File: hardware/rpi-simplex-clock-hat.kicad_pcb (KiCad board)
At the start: 2 copper layers, 65 x 56 mm, 23 parts, among them J1 TBP01R1-508-04BE, J2 Barrel_Jack_Switch, J3 GPIO, U1 LAA120, U2 CAT24C256

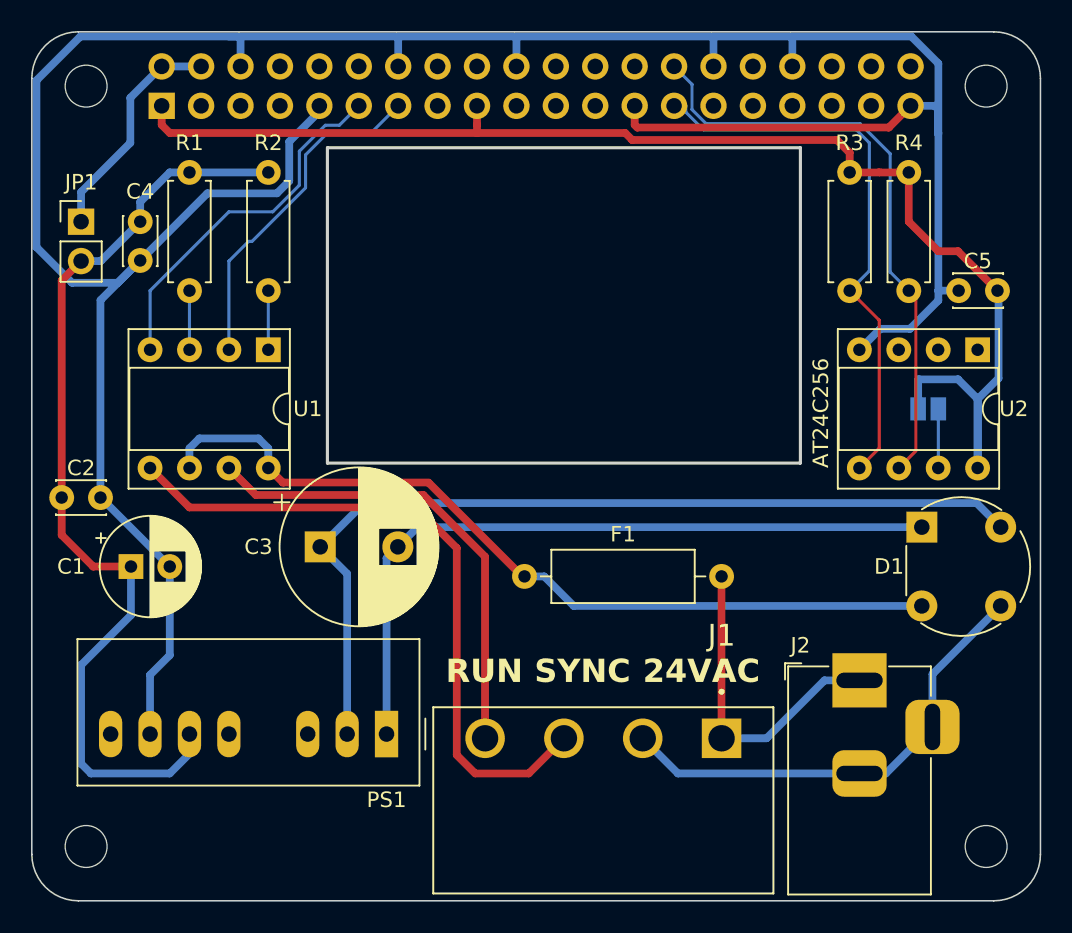
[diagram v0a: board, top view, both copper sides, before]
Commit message: Rev 1: Fix minor issues in Rev 0.
1. Turn SSRs on with logic 1 to GPIO outputs.  This is needed so that
   the SSRs don't become enabled when the GPIO17 and GPIO27 are set to
   outputs.  These GPIOs are pulled low.

2. Add alternate footprint location (J4) for AC input barrel jack.

3. Add additional mounting holes for Raspberry Pi Zero / Zero 2 W.

4. Correct pinout for the bridge rectifier D1.
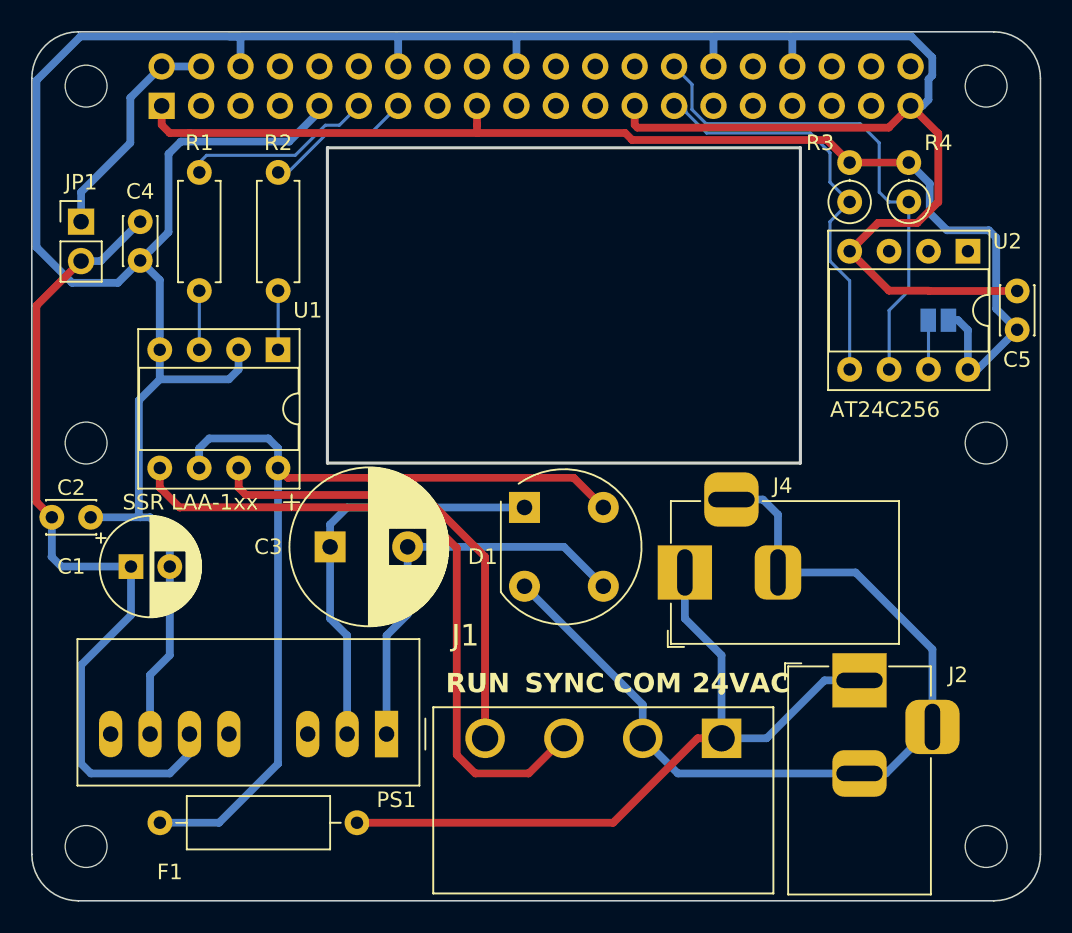
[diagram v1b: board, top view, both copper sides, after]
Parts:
- added J4: Barrel_Jack_Switch, Connector_BarrelJack:BarrelJack_Horizontal, F.Cu at (142.1, 78.8)
- added MH5: MountingHole_2.7mm_M2.5, MountingHole:MountingHole_2.7mm_M2.5, F.Cu at (103.5, 70.5)
- added MH6: MountingHole_2.7mm_M2.5, MountingHole:MountingHole_2.7mm_M2.5, F.Cu at (161.5, 70.5)
- D1: value D_Bridge_-AA+ -> B250C1000G-E4/51; footprint Diode_THT:Diode_Bridge_Round_D8.9mm -> Diode_THT:Diode_Bridge_Round_D9.8mm
- R1, R2: value 330 -> 220
- R3, R4: footprint Resistor_THT:R_Axial_DIN0207_L6.3mm_D2.5mm_P7.62mm_Horizontal -> Resistor_THT:R_Axial_DIN0207_L6.3mm_D2.5mm_P2.54mm_Vertical
- moved F1 28.4 mm to (108.3, 94.9)
- moved D1 25.6 mm to (131.8, 74.6)
- moved U2 6.38 mm to (160.3, 58.1)
- moved JP2 5.75 mm to (158.4, 62.5), turned to 0 degrees
- moved R3 5.72 mm to (152.7, 54.9)
- moved R4 5.72 mm to (156.5, 54.9)
- moved C5 2.82 mm to (163.5, 63.1), turned to 90 degrees
- moved C2 1.42 mm to (101.3, 75.2)
- moved C3 0.64 mm to (119.2, 77.1)
- moved R1 0.64 mm to (110.8, 60.6)
- moved R2 0.64 mm to (115.9, 60.6)
- moved U1 0.62 mm to (115.9, 64.4)
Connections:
- D1 pad 1: /COM -> +48V
- D1 pad 2: AC -> Net-(D1-Pad2)
- D1 pad 3: Net-(D1-Pad3) -> /COM
- D1 pad 4: +48V -> AC
- J1 pad 2: Net-(D1-Pad3) -> Net-(D1-Pad2)
- J2 pad 2: Net-(D1-Pad3) -> Net-(D1-Pad2)
- J2 pad 3: Net-(D1-Pad3) -> Net-(D1-Pad2)
- R1 pad 2: +5V -> /GPIO17
- R2 pad 2: +5V -> /GPIO27
- U1 pad 2: /GPIO27 -> GND
- U1 pad 4: /GPIO17 -> GND
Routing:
- net Net-(D1-Pad2): track 0.00 -> 57.9 mm
- net +48V: track 58.4 -> 26.9 mm
- net Net-(D1-Pad3): track 30.5 -> 0.00 mm
- net /VIN: track 20.9 -> 47.9 mm
- net /COM: track 46.7 -> 26.3 mm
- net GND: track 187.0 -> 200.6 mm
- net /GPIO27: track 22.0 -> 9.51 mm
- net /GPIO17: track 23.5 -> 12.4 mm
- net +3.3V: track 86.6 -> 75.7 mm
- net /ID_SDA: track 36.6 -> 27.1 mm
- net +5V: track 61.7 -> 54.0 mm
- net /ID_SCL: track 38.6 -> 32.9 mm
- net AC: track 53.9 -> 58.4 mm
- net Net-(JP2-A): track 3.81 -> 3.18 mm
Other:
- board text added: "COM"
- board text added: "SSR LAA-1xx"
- board text added: "Simplex Clock Controller Rev 1 https://github.com/hharte/rpi-simplex-clock-hat"
- board text removed: "Simplex Clock Controller Rev 0 https://github.com/hharte/rpi-simplex-clock-hat"

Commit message: Update for KiCAD 8.0
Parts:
- moved C1 0.59 mm to (106.4, 79.0)

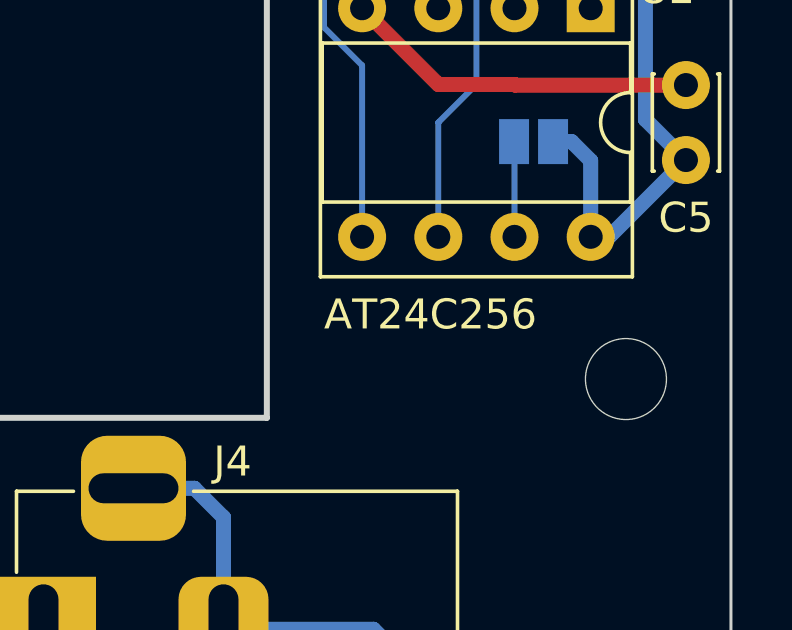
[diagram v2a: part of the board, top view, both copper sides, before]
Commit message: Add interactive BOM, update to KiCAD 8.0.1.
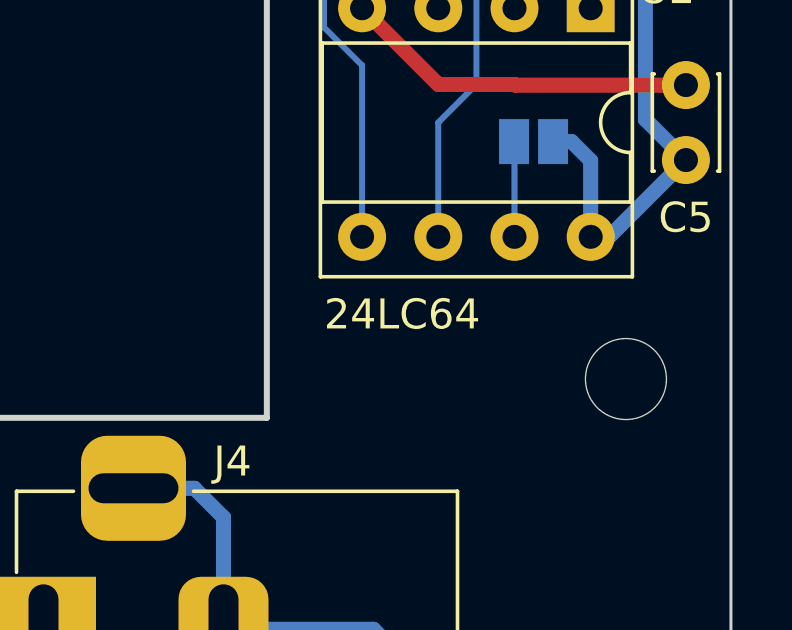
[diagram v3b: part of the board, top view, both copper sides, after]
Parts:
- U1: value LAA120 -> LAA108
- U2: value CAT24C256 -> 24LC64-I/P
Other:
- board text added: "24LC64"
- board text removed: "AT24C256"
